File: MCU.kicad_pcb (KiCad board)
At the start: 4 copper layers, 110.3 x 102.2 mm, 142 parts, among them J1 F31L-1A7H1-11030, J10 Conn_02x10_Odd_Even, J11 Conn_01x10, J12 Conn_01x10, J13 Conn_01x10, J14 Conn_01x10, J15 Conn_01x02, J16 Conn_02x10_Odd_Even, J17 Conn_02x30_Counter_Clockwise, J18 Conn_01x10, J19 Conn_01x10, J2 F31L-1A7H1-11030, J20 Conn_01x02, J21 Conn_02x10_Odd_Even, J3 F31L-1A7H1-11030, J32 Conn_01x02, J4 Conn_02x30_Counter_Clockwise, J5 Conn_02x10_Odd_Even, J6 Conn_01x02, J7 Conn_01x10, J8 Conn_01x10, J9 Conn_01x02, U1 TPS76333, U10 TXB0104RUT, U11 TPS76333, U12 TXB0104RUT, U13 TXB0104RUT, U14 TPS76333, U2 TXB0104RUT, U3 TPS76333, U4 TPS76333, U5 TXB0104RUT, U6 TXB0104RUT, U7 TXB0104RUT, U8 TPS76333, U9 TXB0104RUT

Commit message: Add files via upload
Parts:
- removed R41: 1k, Resistor_SMD:R_0603_1608Metric
- added H5: MountingHole_Pad, MountingHole:MountingHole_2.2mm_M2_DIN965_Pad, F.Cu at (123.6, 142.9)
- added J22: Conn_01x02, Connector_PinHeader_2.54mm:PinHeader_1x02_P2.54mm_Vertical, F.Cu at (185.6, 53.4)
- added R32: 1R, Resistor_SMD:R_0603_1608Metric, F.Cu at (105.1, 104.9)
- R29: value 4k7 -> 0R
- R30: value 9k1 -> 4k7
- R31: value 1R -> 9k1
- R92: value 0R -> 1k
- moved R94 111.4 mm to (156.1, 121.1)
- moved R93 99.1 mm to (157.0, 87.1), turned to 90 degrees
- moved R90 90.3 mm to (154.2, 48.0), turned to 90 degrees
- moved H2 82.3 mm to (95.0, 53.2)
- moved R89 66.5 mm to (130.4, 43.6)
- moved R92 66.3 mm to (108.5, 109.0), turned to 180 degrees
- moved H3 51.0 mm to (112.7, 89.8)
- moved R91 49.7 mm to (116.2, 64.2), turned to -90 degrees
- moved H4 34.5 mm to (152.8, 142.9)
- moved D3 27.7 mm to (128.1, 48.8), turned to 180 degrees
- moved C8 26.3 mm to (131.9, 42.0)
- moved R4 25.8 mm to (155.8, 48.0), turned to -90 degrees
- moved R5 24.6 mm to (157.4, 48.0), turned to 90 degrees
- moved R9 24.3 mm to (133.7, 43.5)
- moved R10 23.4 mm to (133.7, 45.1)
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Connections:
- C12 pad 1: P3V3_LOCAL -> /GP_SUB/P3V3_LOCAL
- C14 pad 1: P3V3_LOCAL -> /GP_SUB/P3V3_LOCAL
- C19 pad 1: P3V3_LOCAL -> /GP_SUB1/P3V3_LOCAL
- C2 pad 1: P3V3_LOCAL -> /GP_SUB/P3V3_LOCAL
- C20 pad 1: P3V3_LOCAL -> /GP_SUB1/P3V3_LOCAL
- C22 pad 1: P3V3_LOCAL -> /GP_SUB1/P3V3_LOCAL
- C25 pad 1: P3V3_LOCAL -> /GP_SUB2/P3V3_LOCAL
- C26 pad 1: P3V3_LOCAL -> /GP_SUB2/P3V3_LOCAL
- C28 pad 1: P3V3_LOCAL -> /GP_SUB2/P3V3_LOCAL
- C31 pad 1: P3V3_LOCAL -> /GP_SUB3/P3V3_LOCAL
- C32 pad 1: P3V3_LOCAL -> /GP_SUB3/P3V3_LOCAL
- C34 pad 1: P3V3_LOCAL -> /GP_SUB3/P3V3_LOCAL
- J11 pad 1: P3V3_LOCAL -> /GP_SUB2/P3V3_LOCAL
- J13 pad 1: P3V3_LOCAL -> /GP_SUB/P3V3_LOCAL
- J15 pad 1: P3V3_LOCAL -> /GP_SUB2/P3V3_LOCAL
- J17 pad 10: unconnected-(J17-Pin_10-Pad10) -> GND
- J17 pad 11: unconnected-(J17-Pin_11-Pad11) -> GND
- J17 pad 12: unconnected-(J17-Pin_12-Pad12) -> GND
- J17 pad 13: unconnected-(J17-Pin_13-Pad13) -> GND
- J17 pad 14: unconnected-(J17-Pin_14-Pad14) -> GND
- J17 pad 15: unconnected-(J17-Pin_15-Pad15) -> GND
- J17 pad 16: unconnected-(J17-Pin_16-Pad16) -> GND
- J17 pad 17: unconnected-(J17-Pin_17-Pad17) -> GND
- J17 pad 18: unconnected-(J17-Pin_18-Pad18) -> GND
- J17 pad 19: unconnected-(J17-Pin_19-Pad19) -> GND
- J17 pad 20: unconnected-(J17-Pin_20-Pad20) -> GND
- J17 pad 21: unconnected-(J17-Pin_21-Pad21) -> GND
- J17 pad 31: unconnected-(J17-Pin_31-Pad31) -> HMI_EN
- J17 pad 32: unconnected-(J17-Pin_32-Pad32) -> PROT_EN
- J17 pad 33: unconnected-(J17-Pin_33-Pad33) -> PD11
- J17 pad 34: unconnected-(J17-Pin_34-Pad34) -> PD10
- J17 pad 35: unconnected-(J17-Pin_35-Pad35) -> PA2_ADCIN7
- J17 pad 36: unconnected-(J17-Pin_36-Pad36) -> PA3_ADCIN8
- J17 pad 37: unconnected-(J17-Pin_37-Pad37) -> PB0_ADCIN15
- J17 pad 38: unconnected-(J17-Pin_38-Pad38) -> PC1_ADCIN2
- J17 pad 39: unconnected-(J17-Pin_39-Pad39) -> PC2_ADCIN3
- J17 pad 40: unconnected-(J17-Pin_40-Pad40) -> PC3_ADCIN4
- J17 pad 41: unconnected-(J17-Pin_41-Pad41) -> PA0_ADCIN5
- J17 pad 42: unconnected-(J17-Pin_42-Pad42) -> PA1_ADCIN6
- J17 pad 43: unconnected-(J17-Pin_43-Pad43) -> GND
- J17 pad 44: unconnected-(J17-Pin_44-Pad44) -> GND
- J17 pad 45: unconnected-(J17-Pin_45-Pad45) -> GND
- J17 pad 46: unconnected-(J17-Pin_46-Pad46) -> GND
- J17 pad 47: unconnected-(J17-Pin_47-Pad47) -> GND
- J17 pad 48: unconnected-(J17-Pin_48-Pad48) -> GND
- J17 pad 49: unconnected-(J17-Pin_49-Pad49) -> GND
- J17 pad 50: unconnected-(J17-Pin_50-Pad50) -> GND
- J17 pad 51: unconnected-(J17-Pin_51-Pad51) -> GND
- J17 pad 52: unconnected-(J17-Pin_52-Pad52) -> GND
- J17 pad 53: unconnected-(J17-Pin_53-Pad53) -> GND
- J17 pad 54: unconnected-(J17-Pin_54-Pad54) -> GND
- J17 pad 55: unconnected-(J17-Pin_55-Pad55) -> GND
- J17 pad 56: unconnected-(J17-Pin_56-Pad56) -> GND
- J17 pad 57: unconnected-(J17-Pin_57-Pad57) -> GND
- J17 pad 58: unconnected-(J17-Pin_58-Pad58) -> GND
- J17 pad 59: unconnected-(J17-Pin_59-Pad59) -> GND
- J17 pad 60: unconnected-(J17-Pin_60-Pad60) -> GND
- J18 pad 1: P3V3_LOCAL -> /GP_SUB3/P3V3_LOCAL
- J20 pad 1: P3V3_LOCAL -> /GP_SUB3/P3V3_LOCAL
- J32 pad 1: P3V3_LOCAL -> /GP_SUB/P3V3_LOCAL
- J4 pad 10: unconnected-(J4-Pin_10-Pad10) -> GND
- J4 pad 11: unconnected-(J4-Pin_11-Pad11) -> GND
- J4 pad 12: unconnected-(J4-Pin_12-Pad12) -> GND
- J4 pad 13: unconnected-(J4-Pin_13-Pad13) -> GND
- J4 pad 14: unconnected-(J4-Pin_14-Pad14) -> GND
- J4 pad 15: unconnected-(J4-Pin_15-Pad15) -> GND
- J4 pad 16: unconnected-(J4-Pin_16-Pad16) -> GND
- J4 pad 17: unconnected-(J4-Pin_17-Pad17) -> GND
- J4 pad 18: unconnected-(J4-Pin_18-Pad18) -> GND
- J4 pad 19: unconnected-(J4-Pin_19-Pad19) -> GND
- J4 pad 20: unconnected-(J4-Pin_20-Pad20) -> GND
- J4 pad 21: unconnected-(J4-Pin_21-Pad21) -> GND
- J4 pad 22: /GP_SUB1/TP16_Pin16 -> GND
- J4 pad 23: /GP_SUB1/TP6_Pin7 -> GND
- J4 pad 24: /GP_SUB1/TP12_Pin8 -> GND
- J4 pad 25: /GP_SUB1/TP13_Pin9 -> GND
- J4 pad 26: /GP_SUB1/TP7_Pin11 -> GND
- J4 pad 27: /GP_SUB1/TP15_Pin12 -> GND
- J4 pad 28: /GP_SUB1/TP8_Pin13 -> GND
- J4 pad 29: /GP_SUB1/TP2_Pin14 -> GND
- J4 pad 30: /GP_SUB1/GP_EN -> GND
- J4 pad 31: unconnected-(J4-Pin_31-Pad31) -> PC13_EXTI13
- J4 pad 32: unconnected-(J4-Pin_32-Pad32) -> PE5_EXTI5
- J4 pad 33: unconnected-(J4-Pin_33-Pad33) -> BRSW_CTL_C
- J4 pad 34: unconnected-(J4-Pin_34-Pad34) -> PD13
- J4 pad 35: unconnected-(J4-Pin_35-Pad35) -> PE3_TIM3_CH1
- J4 pad 36: unconnected-(J4-Pin_36-Pad36) -> PB10_I2C2_SCL
- J4 pad 37: unconnected-(J4-Pin_37-Pad37) -> PB11_I2C2_SDA
- J4 pad 38: unconnected-(J4-Pin_38-Pad38) -> PE6_EXTI6
- J4 pad 39: unconnected-(J4-Pin_39-Pad39) -> PE10_EXTI10
- J4 pad 40: unconnected-(J4-Pin_40-Pad40) -> PD14
- J4 pad 41: unconnected-(J4-Pin_41-Pad41) -> PE2
- J4 pad 42: unconnected-(J4-Pin_42-Pad42) -> GND
- J4 pad 43: unconnected-(J4-Pin_43-Pad43) -> GND
- J4 pad 44: unconnected-(J4-Pin_44-Pad44) -> GND
- J4 pad 45: unconnected-(J4-Pin_45-Pad45) -> GND
- J4 pad 46: unconnected-(J4-Pin_46-Pad46) -> GND
- J4 pad 47: unconnected-(J4-Pin_47-Pad47) -> GND
- J4 pad 48: unconnected-(J4-Pin_48-Pad48) -> GND
- J4 pad 49: unconnected-(J4-Pin_49-Pad49) -> GND
- J4 pad 50: unconnected-(J4-Pin_50-Pad50) -> GND
- J4 pad 51: unconnected-(J4-Pin_51-Pad51) -> GND
- J4 pad 52: unconnected-(J4-Pin_52-Pad52) -> /GP_SUB1/GP_EN
- J4 pad 53: unconnected-(J4-Pin_53-Pad53) -> /GP_SUB1/TP2_Pin14
- J4 pad 54: unconnected-(J4-Pin_54-Pad54) -> /GP_SUB1/TP8_Pin13
- J4 pad 55: unconnected-(J4-Pin_55-Pad55) -> /GP_SUB1/TP15_Pin12
- J4 pad 56: unconnected-(J4-Pin_56-Pad56) -> /GP_SUB1/TP7_Pin11
- J4 pad 57: unconnected-(J4-Pin_57-Pad57) -> /GP_SUB1/TP13_Pin9
- J4 pad 58: unconnected-(J4-Pin_58-Pad58) -> /GP_SUB1/TP12_Pin8
- J4 pad 59: unconnected-(J4-Pin_59-Pad59) -> /GP_SUB1/TP6_Pin7
- J4 pad 60: unconnected-(J4-Pin_60-Pad60) -> /GP_SUB1/TP16_Pin16
- J7 pad 1: P3V3_LOCAL -> /GP_SUB1/P3V3_LOCAL
- J9 pad 1: P3V3_LOCAL -> /GP_SUB1/P3V3_LOCAL
- R29 pad 1: /GP_SUB1/GP_EN -> VBUS
- R29 pad 2: Net-(U8-EN) -> /GP_SUB1/GP_EN
- R30 pad 1: GND -> /GP_SUB1/GP_EN
- R31 pad 1: Net-(C22-Pad2) -> GND
- R31 pad 2: GND -> Net-(U8-EN)
- R68 pad 2: P3V3_LOCAL -> /GP_SUB2/P3V3_LOCAL
- R8 pad 2: P3V3_LOCAL -> /GP_SUB/P3V3_LOCAL
- R88 pad 2: P3V3_LOCAL -> /GP_SUB3/P3V3_LOCAL
- R92 pad 1: VBUS -> Net-(D4-A)
- R92 pad 2: /GP_SUB1/GP_EN -> /GP_SUB1/P3V3_LOCAL
- U1 pad 5: P3V3_LOCAL -> /GP_SUB/P3V3_LOCAL
- U10 pad 1: P3V3_LOCAL -> /GP_SUB2/P3V3_LOCAL
- U10 pad 12: P3V3_LOCAL -> /GP_SUB2/P3V3_LOCAL
- U11 pad 5: P3V3_LOCAL -> /GP_SUB2/P3V3_LOCAL
- U12 pad 1: P3V3_LOCAL -> /GP_SUB3/P3V3_LOCAL
- U12 pad 12: P3V3_LOCAL -> /GP_SUB3/P3V3_LOCAL
- U13 pad 1: P3V3_LOCAL -> /GP_SUB3/P3V3_LOCAL
- U13 pad 12: P3V3_LOCAL -> /GP_SUB3/P3V3_LOCAL
- U14 pad 5: P3V3_LOCAL -> /GP_SUB3/P3V3_LOCAL
- U2 pad 1: P3V3_LOCAL -> /GP_SUB/P3V3_LOCAL
- U2 pad 12: P3V3_LOCAL -> /GP_SUB/P3V3_LOCAL
- U5 pad 1: P3V3_LOCAL -> /GP_SUB/P3V3_LOCAL
- U5 pad 12: P3V3_LOCAL -> /GP_SUB/P3V3_LOCAL
- U6 pad 1: P3V3_LOCAL -> /GP_SUB1/P3V3_LOCAL
- U6 pad 12: P3V3_LOCAL -> /GP_SUB1/P3V3_LOCAL
- U7 pad 1: P3V3_LOCAL -> /GP_SUB1/P3V3_LOCAL
- U7 pad 12: P3V3_LOCAL -> /GP_SUB1/P3V3_LOCAL
- U8 pad 5: P3V3_LOCAL -> /GP_SUB1/P3V3_LOCAL
- U9 pad 1: P3V3_LOCAL -> /GP_SUB2/P3V3_LOCAL
- U9 pad 12: P3V3_LOCAL -> /GP_SUB2/P3V3_LOCAL
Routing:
- net PB14_SPI2_MISO: track 19.6 -> 322.5 mm
- net PB13_SPI2_SCK: track 17.5 -> 259.9 mm, vias 0 -> 1
- net PD11: track 0.00 -> 198.1 mm, vias 0 -> 1
- net PB15_SPI2_MOSI: track 24.7 -> 208.3 mm
- net PE6_EXTI6: track 0.00 -> 169.8 mm, vias 0 -> 1
- net PD15_EXTI15: track 19.1 -> 180.0 mm, vias 0 -> 1
- net PC1_ADCIN2: track 0.00 -> 150.8 mm
- net PE12_EXTI12: track 24.1 -> 173.0 mm, vias 0 -> 1
- net PE3_TIM3_CH1: track 0.00 -> 144.7 mm, vias 0 -> 1
- net PC2_ADCIN3: track 0.00 -> 138.8 mm
- net GND: track 77.5 -> 216.3 mm, vias 45 -> 67
- net BRSW_CTL_C: track 0.00 -> 129.9 mm, vias 0 -> 1
- net PD14: track 0.00 -> 127.7 mm, vias 0 -> 2
- net PE9_EXTI9: track 24.1 -> 149.8 mm, vias 0 -> 1
- net PC3_ADCIN4: track 0.00 -> 118.8 mm
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- added copper zone on In2.Cu, net /GP_SUB/P3V3_LOCAL
- added copper zone on In2.Cu, net /GP_SUB1/P3V3_LOCAL
- added copper zone on In2.Cu, net /GP_SUB2/P3V3_LOCAL
- added copper zone on In2.Cu, net /GP_SUB3/P3V3_LOCAL
- added copper zone on F.Cu, net VBUS
- removed copper zone on In2.Cu, net P3V3_LOCAL
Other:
- board size 110.3 x 102.2 mm -> 110.3 x 115 mm
- board text added: "GND"
- board text added: "VBUS"

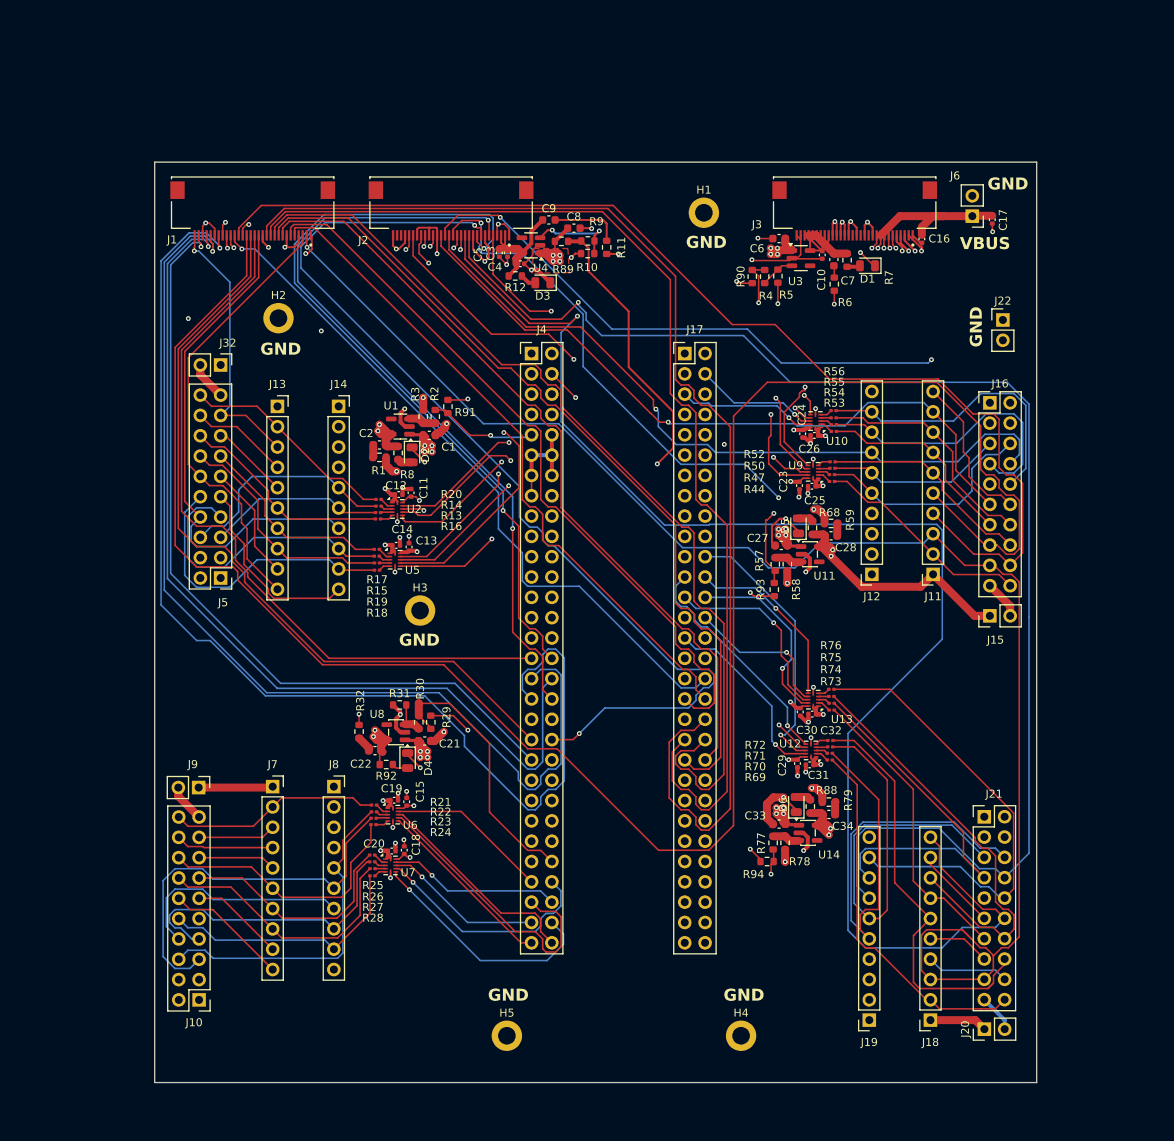
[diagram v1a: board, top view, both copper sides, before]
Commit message: Rails alim + libs
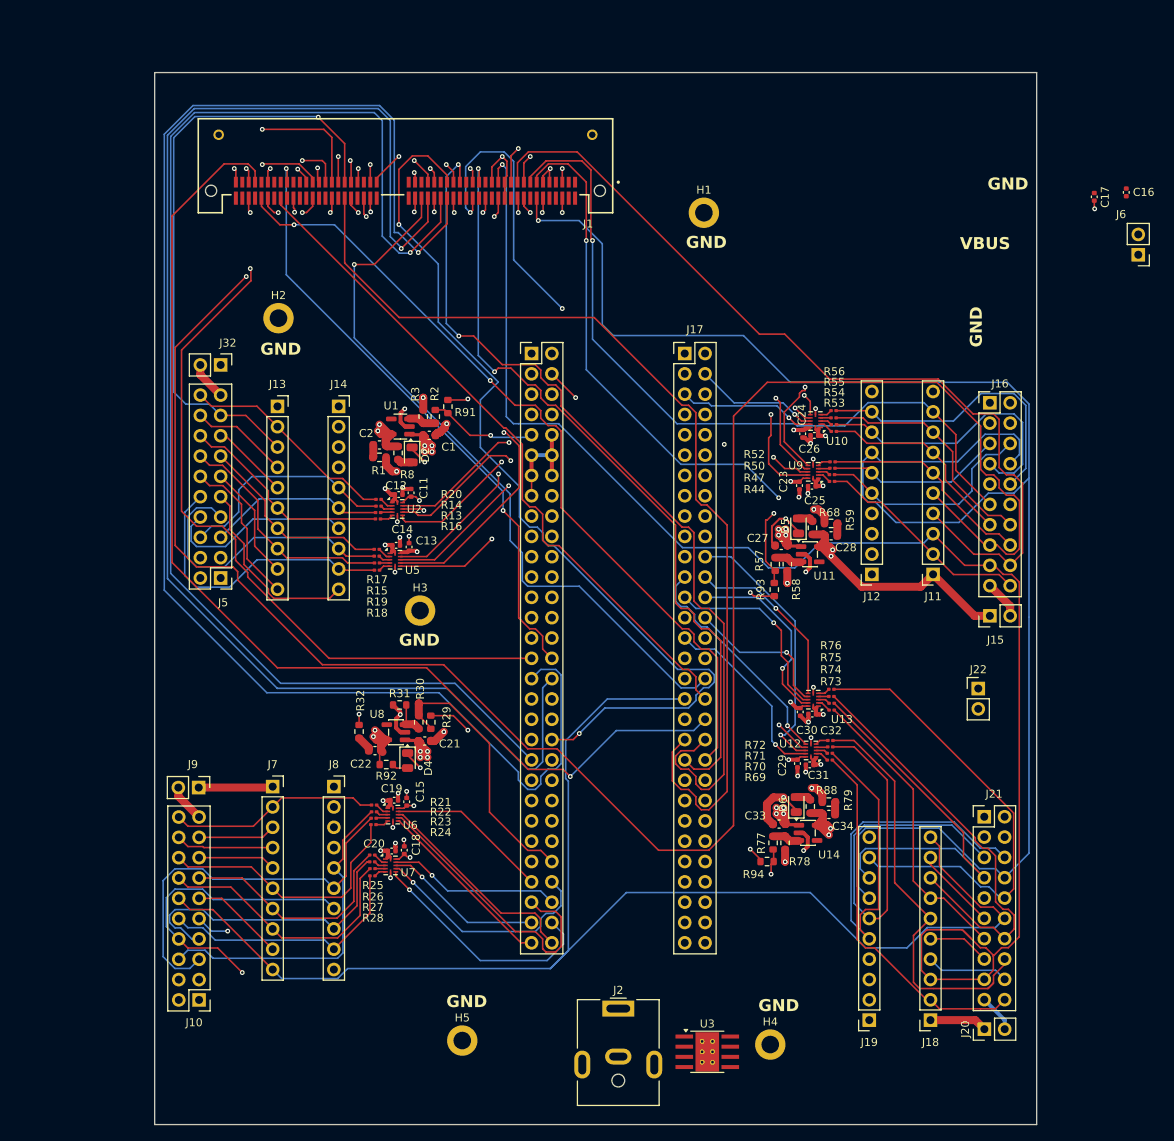
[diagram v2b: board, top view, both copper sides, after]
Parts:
- removed C10, C3, C5: 100nF, Capacitor_SMD:C_0402_1005Metric
- removed C4: 4.7uF, Capacitor_SMD:C_0402_1005Metric
- removed C6, C8: 1uF, Capacitor_SMD:C_0603_1608Metric
- removed C7, C9: 4.7uF, Capacitor_SMD:C_0603_1608Metric
- removed D1, D3: LED, LED_SMD:LED_0805_2012Metric
- removed J3: F31L-1A7H1-11030, F31L-1A7H1-11030:AMPHENOL_F31L-1A7H1-11030
- removed R10, R5: 9k1, Resistor_SMD:R_0603_1608Metric
- removed R11, R6, R89, R90: 1R, Resistor_SMD:R_0603_1608Metric
- removed R12, R7: 1k, Resistor_SMD:R_0603_1608Metric
- removed R4, R9: 4k7, Resistor_SMD:R_0603_1608Metric
- removed U4: TPS76333, Package_TO_SOT_SMD:SOT-23-5
- J1: value F31L-1A7H1-11030 -> HSEC8-150-01-X-RA-X; footprint F31L-1A7H1-11030:AMPHENOL_F31L-1A7H1-11030 -> kicad_jlcpcb_hil_mcu_ep2:SAMTEC_HSEC8-150-01-X-RA-X
- J2: value F31L-1A7H1-11030 -> Barrel_Jack_MountingPin; footprint F31L-1A7H1-11030:AMPHENOL_F31L-1A7H1-11030 -> Connector_BarrelJack:BarrelJack_CUI_PJ-063AH_Horizontal
- U3: value TPS76333 -> LMR36510ADDA; footprint Package_TO_SOT_SMD:SOT-23-5 -> Package_SO:Texas_HTSOP-8-1EP_3.9x4.9mm_P1.27mm_EP2.95x4.9mm_Mask2.4x3.1mm_ThermalVias
- moved J2 102.9 mm to (137.5, 139.5), turned to 0 degrees
- moved U3 99.9 mm to (148.6, 144.9)
- moved J22 46.2 mm to (182.5, 99.5)
- moved C16 26.2 mm to (201.0, 37.5)
- moved J6 21.3 mm to (202.5, 45.3)
- moved J1 19.2 mm to (110.9, 37.3)
- moved C17 13.1 mm to (197.0, 38.0)
- moved H5 5.61 mm to (118.0, 143.5)
- moved H4 3.81 mm to (156.5, 144.0)
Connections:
- net PB15_SPI2_MOSI renamed DS_MOSI
- C1 pad 1: VBUS -> P5VAN
- C1 pad 2: GND -> A0V
- C11 pad 1: VBUS -> P5VAN
- C11 pad 2: GND -> A0V
- C12 pad 2: GND -> A0V
- C13 pad 1: VBUS -> P5VAN
- C13 pad 2: GND -> A0V
- C14 pad 2: GND -> A0V
- C15 pad 1: VBUS -> P5VAN
- C15 pad 2: GND -> A0V
- C16 pad 2: GND -> A0V
- C17 pad 2: GND -> A0V
- C18 pad 1: VBUS -> P5VAN
- C18 pad 2: GND -> A0V
- C19 pad 2: GND -> A0V
- C20 pad 2: GND -> A0V
- C21 pad 1: VBUS -> P5VAN
- C21 pad 2: GND -> A0V
- C23 pad 1: VBUS -> P5VAN
- C23 pad 2: GND -> A0V
- C24 pad 1: VBUS -> P5VAN
- C24 pad 2: GND -> A0V
- C25 pad 2: GND -> A0V
- C26 pad 2: GND -> A0V
- C27 pad 1: VBUS -> P5VAN
- C27 pad 2: GND -> A0V
- C29 pad 1: VBUS -> P5VAN
- C29 pad 2: GND -> A0V
- C30 pad 1: VBUS -> P5VAN
- C30 pad 2: GND -> A0V
- C31 pad 2: GND -> A0V
- C32 pad 2: GND -> A0V
- C33 pad 1: VBUS -> P5VAN
- C33 pad 2: GND -> A0V
- D2 pad 1: GND -> A0V
- D4 pad 1: GND -> A0V
- D5 pad 1: GND -> A0V
- D6 pad 1: GND -> A0V
- H1 pad 1: GND -> A0V
- H2 pad 1: GND -> A0V
- H3 pad 1: GND -> A0V
- H4 pad 1: GND -> A0V
- H5 pad 1: GND -> A0V
- J1 pad 10: PC3_ADCIN4 -> unconnected-(J1-Pad10)
- J1 pad 11: PC2_ADCIN3 -> A0V
- J1 pad 12: PC1_ADCIN2 -> A0V
- J1 pad 13: GND -> DS_NCS_C2
- J1 pad 14: PC0_EXTI0 -> OPCL_DS
- J1 pad 15: PC13_EXTI13 -> DS_NCS_C1
- J1 pad 16: PE10_EXTI10 -> unconnected-(J1-Pad16)
- J1 pad 17: PB14_SPI2_MISO -> A0V
- J1 pad 18: GND -> A0V
- J1 pad 20: PD10 -> BTN_TRIP_TEST
- J1 pad 21: PD11 -> DS_MISO
- J1 pad 22: PE6_EXTI6 -> unconnected-(J1-Pad22)
- J1 pad 23: GND -> A0V
- J1 pad 24: PE3_TIM3_CH1 -> A0V
- J1 pad 25: GND -> DS_SCLK
- J1 pad 26: BRSW_CTL_C -> SDMOS
- J1 pad 27: PD13 -> A0V
- J1 pad 28: GND -> unconnected-(J1-Pad28)
- J1 pad 29: PE2 -> unconnected-(J1-Pad29)
- J1 pad 30: PE13_SPI1_SCK -> A0V
- J10 pad 11: PE7 -> US_NCS_C2
- J10 pad 12: PE8 -> SDMOS
- J10 pad 15: PE14_SPI1_MISO -> US_MISO
- J10 pad 17: PE13_SPI1_SCK -> US_SCLK
- J10 pad 18: PA7_SPI1_MOSI -> US_MOSI
- J10 pad 8: PE9_EXTI9 -> OPCL_US
- J10 pad 9: GND -> A0V
- J11 pad 10: PA9 -> SDMOS
- J11 pad 3: PB13_SPI2_SCK -> DS_SCLK
- J11 pad 5: PB14_SPI2_MISO -> DS_MISO
- J11 pad 9: PC6 -> DS_NCS_C1
- J12 pad 10: GND -> A0V
- J12 pad 7: PA10 -> OPCL_DS
- J13 pad 10: PB2_EXTI2 -> SDMOS
- J13 pad 3: PE13_SPI1_SCK -> US_SCLK
- J13 pad 4: PA7_SPI1_MOSI -> US_MOSI
- J13 pad 5: PE14_SPI1_MISO -> US_MISO
- J13 pad 9: PB1_EXTI1 -> US_NCS_C1
- J14 pad 10: GND -> A0V
- J14 pad 7: PC0_EXTI0 -> OPCL_US
- J16 pad 11: PC6 -> DS_NCS_C1
- J16 pad 12: PA9 -> SDMOS
- J16 pad 15: PB14_SPI2_MISO -> DS_MISO
- J16 pad 17: PB13_SPI2_SCK -> DS_SCLK
- J16 pad 8: PA10 -> OPCL_DS
- J16 pad 9: GND -> A0V
- J17 pad 10: GND -> A0V
- J17 pad 11: GND -> A0V
- J17 pad 12: GND -> A0V
- J17 pad 13: GND -> A0V
- J17 pad 14: GND -> A0V
- J17 pad 15: GND -> A0V
- J17 pad 16: GND -> A0V
- J17 pad 17: GND -> A0V
- J17 pad 18: GND -> A0V
- J17 pad 19: GND -> A0V
- J17 pad 20: GND -> A0V
- J17 pad 21: GND -> A0V
- J17 pad 31: HMI_EN -> unconnected-(J17-Pin_31-Pad31)
- J17 pad 32: PROT_EN -> unconnected-(J17-Pin_32-Pad32)
- J17 pad 33: PD11 -> unconnected-(J17-Pin_33-Pad33)
- J17 pad 34: PD10 -> ISOSW_HOLD_CMD
- J17 pad 35: PA2_ADCIN7 -> SDMOS
- J17 pad 36: PA3_ADCIN8 -> LEM_DS_IN
- J17 pad 37: PB0_ADCIN15 -> V_CTANK
- J17 pad 38: PC1_ADCIN2 -> V_HERMES
- J17 pad 39: PC2_ADCIN3 -> V_ACT
- J17 pad 40: PC3_ADCIN4 -> V_DS
- J17 pad 41: PA0_ADCIN5 -> V_US
- J17 pad 42: PA1_ADCIN6 -> LEM_US_IN
- J17 pad 43: GND -> A0V
- J17 pad 44: GND -> A0V
- J17 pad 45: GND -> A0V
- J17 pad 46: GND -> A0V
- J17 pad 47: GND -> A0V
- J17 pad 48: GND -> A0V
- J17 pad 49: GND -> A0V
- J17 pad 50: GND -> A0V
- J17 pad 51: GND -> A0V
- J17 pad 52: GND -> A0V
- J17 pad 53: GND -> A0V
- J17 pad 54: GND -> A0V
- J17 pad 55: GND -> A0V
- J17 pad 56: GND -> A0V
- J17 pad 57: GND -> A0V
- J17 pad 58: GND -> A0V
- J17 pad 59: GND -> A0V
- J17 pad 60: GND -> A0V
- J18 pad 10: PD15_EXTI15 -> SDMOS
- J18 pad 3: PB13_SPI2_SCK -> DS_SCLK
- J18 pad 5: PB14_SPI2_MISO -> DS_MISO
- J18 pad 9: PD4 -> DS_NCS_C2
- J19 pad 10: GND -> A0V
- J19 pad 7: PE12_EXTI12 -> OPCL_DS
- J2 pad 1: GND -> P24V
- J2 pad 2: Net-(U4-VOUT) -> unconnected-(J2-Pad2)
- J21 pad 11: PD4 -> DS_NCS_C2
- J21 pad 12: PD15_EXTI15 -> SDMOS
- J21 pad 15: PB14_SPI2_MISO -> DS_MISO
- J21 pad 17: PB13_SPI2_SCK -> DS_SCLK
- J21 pad 8: PE12_EXTI12 -> OPCL_DS
- J21 pad 9: GND -> A0V
- J22 pad 1: GND -> A0V
- J22 pad 2: GND -> A0V
- J4 pad 10: GND -> A0V
- J4 pad 11: GND -> A0V
- J4 pad 12: GND -> A0V
- J4 pad 13: GND -> A0V
- J4 pad 14: GND -> A0V
- J4 pad 15: GND -> A0V
- J4 pad 16: GND -> A0V
- J4 pad 17: GND -> A0V
- J4 pad 18: GND -> A0V
- J4 pad 19: GND -> A0V
- J4 pad 20: GND -> A0V
- J4 pad 21: GND -> A0V
- J4 pad 22: GND -> A0V
- J4 pad 23: GND -> A0V
- J4 pad 24: GND -> A0V
- J4 pad 25: GND -> A0V
- J4 pad 26: GND -> A0V
- J4 pad 27: GND -> A0V
- J4 pad 28: GND -> A0V
- J4 pad 29: GND -> A0V
- J4 pad 30: GND -> A0V
- J4 pad 31: PC13_EXTI13 -> EN_PS_ACT
- J4 pad 32: PE5_EXTI5 -> CTANK_CH_DISCH
- J4 pad 33: BRSW_CTL_C -> ISOSW_OF_ST
- J4 pad 34: PD13 -> PADLOCK_OF
- J4 pad 35: PE3_TIM3_CH1 -> unconnected-(J4-Pin_35-Pad35)
- J4 pad 36: PB10_I2C2_SCL -> unconnected-(J4-Pin_36-Pad36)
- J4 pad 37: PB11_I2C2_SDA -> VPS_P24V_PG
- J4 pad 38: PE6_EXTI6 -> BTN_TRIP_TEST
- J4 pad 40: PD14 -> SSR_CTL
- J4 pad 41: PE2 -> ISOSW_INRUSH_CMD
- J4 pad 42: GND -> A0V
- J4 pad 43: GND -> A0V
- J4 pad 44: GND -> A0V
- J4 pad 45: GND -> A0V
- J4 pad 46: GND -> A0V
- J4 pad 47: GND -> A0V
- J4 pad 48: GND -> A0V
- J4 pad 49: GND -> A0V
- J4 pad 50: GND -> A0V
- J4 pad 51: GND -> A0V
- J5 pad 11: PB1_EXTI1 -> US_NCS_C1
- J5 pad 12: PB2_EXTI2 -> SDMOS
- J5 pad 15: PE14_SPI1_MISO -> US_MISO
- J5 pad 17: PE13_SPI1_SCK -> US_SCLK
- J5 pad 18: PA7_SPI1_MOSI -> US_MOSI
- J5 pad 8: PC0_EXTI0 -> OPCL_US
- J5 pad 9: GND -> A0V
- J6 pad 2: GND -> A0V
- J7 pad 10: PE8 -> SDMOS
- J7 pad 3: PE13_SPI1_SCK -> US_SCLK
- J7 pad 4: PA7_SPI1_MOSI -> US_MOSI
- J7 pad 5: PE14_SPI1_MISO -> US_MISO
- J7 pad 9: PE7 -> US_NCS_C2
- J8 pad 10: GND -> A0V
- J8 pad 7: PE9_EXTI9 -> OPCL_US
- R1 pad 2: GND -> A0V
- R29 pad 1: VBUS -> P5VAN
- R3 pad 1: GND -> A0V
- R31 pad 1: GND -> A0V
- R32 pad 2: GND -> A0V
- R58 pad 1: GND -> A0V
- R59 pad 2: GND -> A0V
- R78 pad 1: GND -> A0V
- R79 pad 2: GND -> A0V
- R91 pad 1: VBUS -> P5VAN
- R93 pad 1: VBUS -> P5VAN
- R94 pad 1: VBUS -> P5VAN
- U1 pad 1: VBUS -> P5VAN
- U1 pad 2: GND -> A0V
- U10 pad 11: VBUS -> P5VAN
- U10 pad 6: GND -> A0V
- U11 pad 1: VBUS -> P5VAN
- U11 pad 2: GND -> A0V
- U12 pad 11: VBUS -> P5VAN
- U12 pad 6: GND -> A0V
- U13 pad 11: VBUS -> P5VAN
- U13 pad 6: GND -> A0V
- U14 pad 1: VBUS -> P5VAN
- U14 pad 2: GND -> A0V
- U2 pad 11: VBUS -> P5VAN
- U2 pad 6: GND -> A0V
- U3 pad 1: VBUS -> unconnected-(U3-PGND-Pad1)
- U3 pad 2: GND -> unconnected-(U3-VIN-Pad2)
- U3 pad 3: Net-(U3-EN) -> unconnected-(U3-EN-Pad3)
- U3 pad 5: +3.3V -> unconnected-(U3-FB-Pad5)
- U5 pad 11: VBUS -> P5VAN
- U5 pad 6: GND -> A0V
- U6 pad 11: VBUS -> P5VAN
- U6 pad 6: GND -> A0V
- U7 pad 11: VBUS -> P5VAN
- U7 pad 6: GND -> A0V
- U8 pad 1: VBUS -> P5VAN
- U8 pad 2: GND -> A0V
- U9 pad 11: VBUS -> P5VAN
- U9 pad 6: GND -> A0V
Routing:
- net SDMOS: track 0.00 -> 485.4 mm, vias 0 -> 1
- net DS_MISO: track 0.00 -> 368.2 mm, vias 0 -> 2
- net VBUS: track 324.2 -> 0.00 mm, vias 42 -> 0
- net P5VAN: track 0.00 -> 323.0 mm, vias 0 -> 29
- net PB14_SPI2_MISO: track 322.5 -> 0.00 mm
- net PB13_SPI2_SCK: track 259.9 -> 0.00 mm, vias 1 -> 0
- net DS_SCLK: track 0.00 -> 258.8 mm, vias 0 -> 1
- net OPCL_US: track 0.00 -> 252.0 mm, vias 0 -> 2
- net BTN_TRIP_TEST: track 0.00 -> 238.8 mm, vias 0 -> 1
- net OPCL_DS: track 0.00 -> 224.4 mm, vias 0 -> 1
- net GND: track 216.3 -> 0.00 mm, vias 67 -> 0
- net PD11: track 198.1 -> 0.00 mm, vias 1 -> 0
- net ISOSW_OF_ST: track 0.00 -> 192.3 mm, vias 0 -> 1
- net A0V: track 0.00 -> 186.4 mm, vias 0 -> 68
- net PD15_EXTI15: track 180.0 -> 0.00 mm, vias 1 -> 0
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- added copper zone on In1.Cu, net A0V
- added copper zone on In2.Cu, net P5VAN
- removed copper zone on In1.Cu, net GND
- removed copper zone on F.Cu, net VBUS
- removed copper zone on In2.Cu, net VBUS
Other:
- board size 110.3 x 115 mm -> 110.3 x 131.5 mm

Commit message: Power
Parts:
- removed C17: 100nF, Capacitor_SMD:C_0402_1005Metric
- added C3: 1uF, Capacitor_SMD:C_0603_1608Metric, F.Cu at (114.9, 140.8)
- added C35: 18pF, Capacitor_SMD:C_0402_1005Metric, F.Cu at (127.0, 138.0)
- added C36: 100nF, Capacitor_SMD:C_0603_1608Metric, F.Cu at (111.5, 140.5)
- added C37: 18pF, Capacitor_SMD:C_0603_1608Metric, F.Cu at (117.5, 136.5)
- added C4: 10uF, Capacitor_SMD:C_0603_1608Metric, F.Cu at (127.0, 140.3)
- added C5: 22uF, Capacitor_SMD:C_0603_1608Metric, F.Cu at (104.5, 148.5)
- added C6: 22uF, Capacitor_SMD:C_0603_1608Metric, F.Cu at (102.7, 148.5)
- added L1: 22uH, Inductor_SMD:L_TDK_SLF10145, F.Cu at (111.0, 147.0)
- added R89: 25.5k, Resistor_SMD:R_0603_1608Metric, F.Cu at (120.0, 137.5)
- added R90: 102k, Resistor_SMD:R_0603_1608Metric, F.Cu at (116.0, 138.3)
- added R95: 33k, Resistor_SMD:R_0603_1608Metric, F.Cu at (130.5, 139.0)
- added R96: 499k, Resistor_SMD:R_0603_1608Metric, F.Cu at (129.0, 137.0)
- added R97: 10k, Resistor_SMD:R_0603_1608Metric, F.Cu at (124.0, 136.3)
- added R98: 15k, Resistor_SMD:R_0603_1608Metric, F.Cu at (125.5, 136.5)
- C16: value 4.7uF -> 100nF; footprint Capacitor_SMD:C_0402_1005Metric -> Capacitor_SMD:C_0603_1608Metric
- moved C16 131.3 mm to (125.0, 144.5), turned to 180 degrees
- moved J6 110.7 mm to (145.5, 140.2), turned to 0 degrees
- moved H1 90.8 mm to (156.0, 130.5)
- moved H2 86.7 mm to (181.5, 47.0)
- moved H5 31.6 mm to (86.5, 146.0)
- moved U3 27.9 mm to (121.0, 141.0), turned to 180 degrees
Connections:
- C16 pad 1: VBUS -> P24V
- J1 pad 02: P3V7 -> P5VAN
- J1 pad 04: P3V7 -> P5VAN
- J1 pad 100: NEG10VAN -> A0V
- J1 pad 98: NEG10VAN -> A0V
- J2 pad 2: unconnected-(J2-Pad2) -> A0V
- J2 pad MP: unconnected-(J2-MountPin-PadMP) -> A0V
- J6 pad 1: VBUS -> P24V
- U3 pad 1: unconnected-(U3-PGND-Pad1) -> A0V
- U3 pad 2: unconnected-(U3-VIN-Pad2) -> P24V
- U3 pad 3: unconnected-(U3-EN-Pad3) -> Net-(U3-EN)
- U3 pad 4: unconnected-(U3-PG-Pad4) -> Net-(U3-PG)
- U3 pad 5: unconnected-(U3-FB-Pad5) -> Net-(U3-FB)
- U3 pad 6: unconnected-(U3-VCC-Pad6) -> Net-(U3-VCC)
- U3 pad 7: unconnected-(U3-BOOT-Pad7) -> Net-(U3-BOOT)
- U3 pad 8: P5VAN -> Net-(U3-SW)
- U3 pad 9: unconnected-(U3-PAD-Pad9) -> A0V
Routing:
- net A0V: track 186.4 -> 247.5 mm, vias 68 -> 84
- net BTN_TRIP_TEST: track 238.8 -> 187.6 mm, vias 1 -> 3
- net P5VAN: track 323.0 -> 357.4 mm, vias 29 -> 46
- net P24V: track 160.2 -> 179.6 mm, vias 1 -> 5
- net Net-(U3-SW): track 0.00 -> 8.40 mm
- net ISOSW_OF_ST: track 192.3 -> 200.6 mm
- net Net-(U3-EN): track 0.00 -> 7.82 mm
- net Net-(U3-BOOT): track 0.00 -> 6.40 mm
- net Net-(U3-FB): track 0.00 -> 6.05 mm
- net ISOSW_INRUSH_CMD: track 164.7 -> 170.4 mm
- net PADLOCK_OF: track 177.7 -> 183.3 mm
- net SSR_CTL: track 117.8 -> 122.2 mm
- net Net-(U3-PG): track 0.00 -> 3.57 mm
- net Net-(U3-VCC): track 0.00 -> 2.66 mm
- net EN_PS_ACT: track 116.7 -> 119.0 mm
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- added copper zone on F.Cu, net Net-(U3-SW)
- added copper zone on F.Cu, net P24V
- added copper zone on F.Cu, net P5VAN
